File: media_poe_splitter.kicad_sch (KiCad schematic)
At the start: 81 parts, among them IC1 LAN7850-I_8JX, IC2 17791063215, IC3 93AA66C-I/SN, J1 Screw_Terminal_01x02, Q1 DMP3099L-7, X1 7499811120, X2 68710614522, Y1 830055299

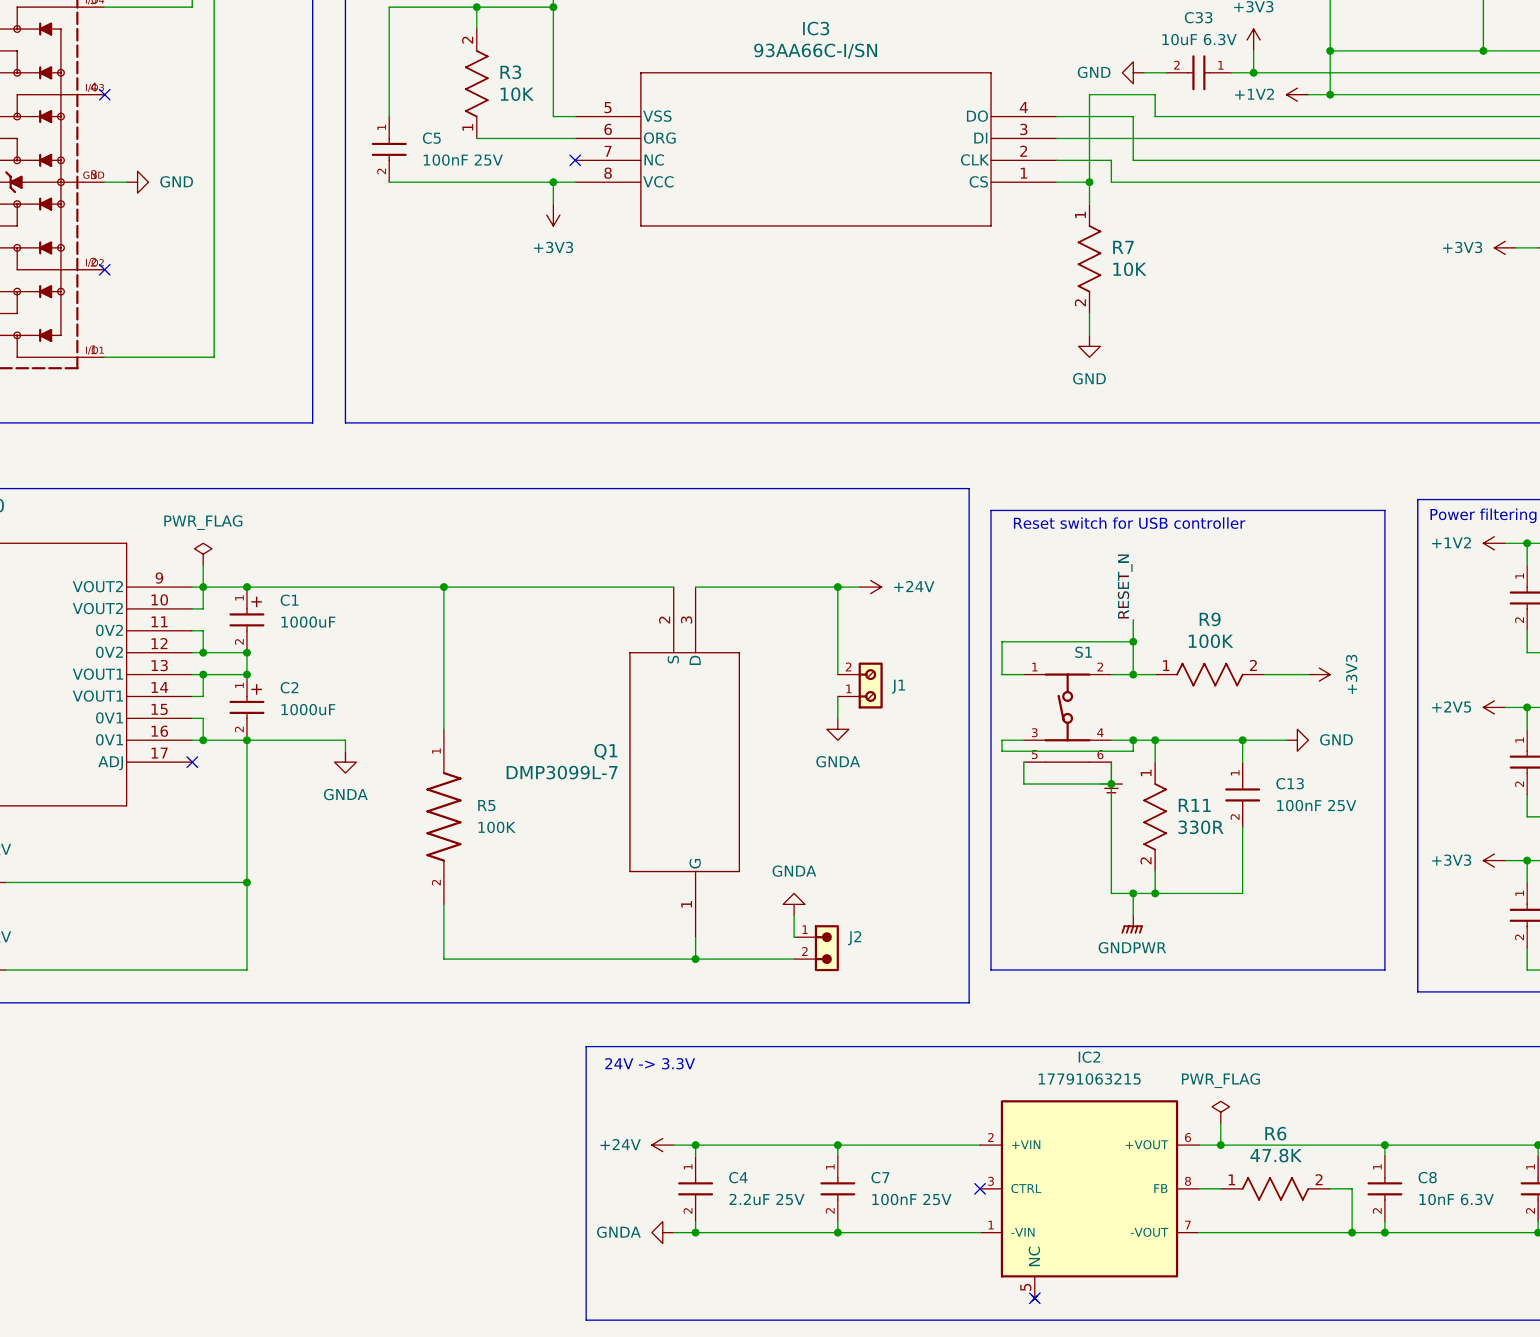
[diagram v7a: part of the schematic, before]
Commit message: board, schematic: try to comply with ERC and DRC
Signed-off-by: Marc 'risson' Schmitt <marc.schmitt@risson.space>
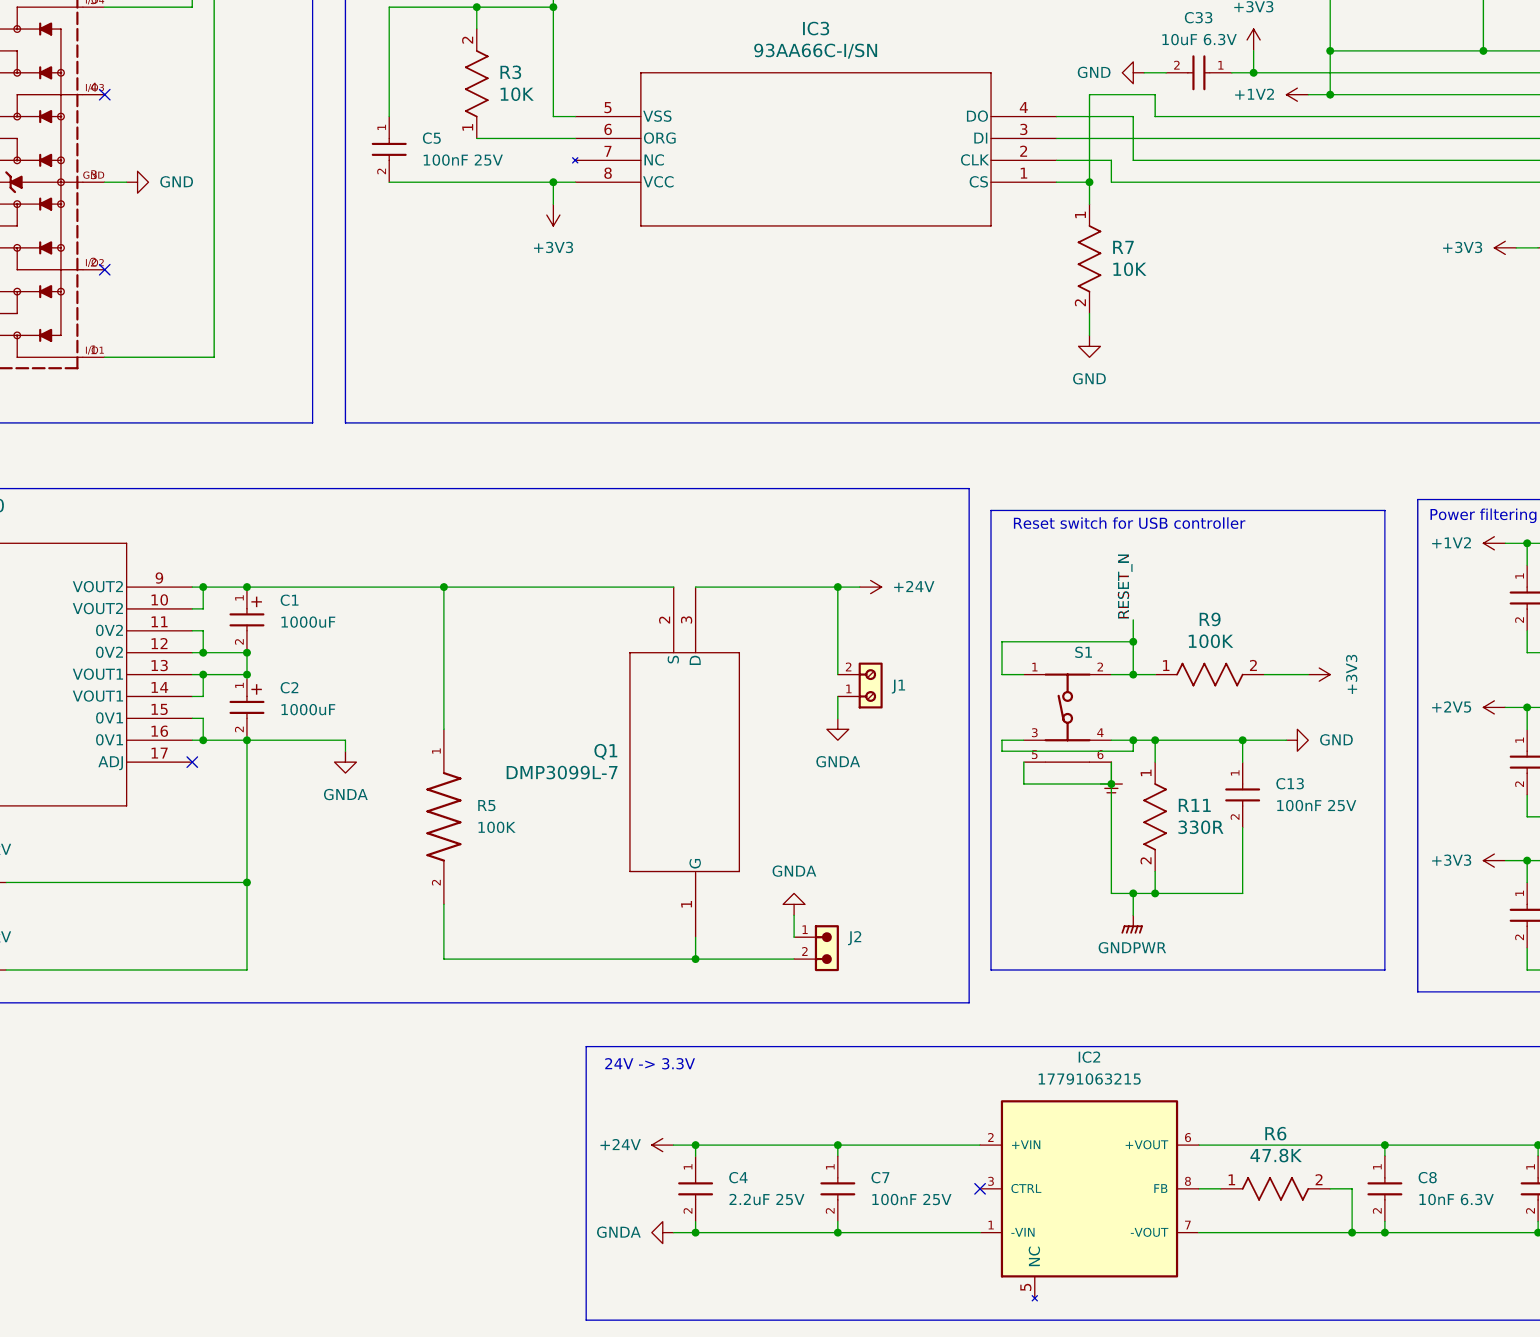
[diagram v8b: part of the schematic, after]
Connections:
- no-connect marks 35 -> 33
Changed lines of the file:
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@@
 	)
 	(junction
-		(at 311.15 276.86)
-		(diameter 0)
-		(color 0 0 0 0)
-	)
-	(junction
 		(at 100.33 116.84)
 		(diameter 0)
@@
 	)
 	(no_connect
-		(at 236.22 162.56)
-	)
-	(no_connect
 		(at 140.97 232.41)
 	)
@@
 	)
 	(no_connect
-		(at 289.56 294.64)
-	)
-	(no_connect
 		(at 457.2 201.93)
 	)
@@
 	(wire
 		(pts
-			(xy 311.15 276.86) (xy 330.2 276.86)
-		)
-		(stroke
-			(width 0)
-			(type default)
-		)
-	)
-	(wire
-		(pts
 			(xy 323.85 149.86) (xy 341.63 149.86)
 		)
@@
 	(wire
 		(pts
-			(xy 308.61 276.86) (xy 311.15 276.86)
+			(xy 308.61 276.86) (xy 330.2 276.86)
 		)
 		(stroke
@@
 	(wire
 		(pts
-			(xy 311.15 274.32) (xy 311.15 276.86)
-		)
-		(stroke
-			(width 0)
-			(type default)
-		)
-	)
-	(wire
-		(pts
 			(xy 359.41 256.54) (xy 372.11 256.54)
 		)
@@
 	(wire
 		(pts
-			(xy 193.04 209.55) (xy 193.04 212.09)
-		)
-		(stroke
-			(width 0)
-			(type default)
-		)
-	)
-	(wire
-		(pts
 			(xy 292.1 160.02) (xy 373.38 160.02)
 		)
@@
 	)
 	(symbol
-		(lib_id "power:PWR_FLAG")
-		(at 193.04 209.55 0)
-		(unit 1)
-		(exclude_from_sim no)
-		(in_bom yes)
-		(on_board yes)
-		(dnp no)
-		(fields_autoplaced yes)
-		(property "Reference" "#FLG01"
-			(at 193.04 207.645 0)
-			(effects
-				(font
-					(size 1.27 1.27)
-				)
-				(hide yes)
-			)
-		)
-		(property "Value" "PWR_FLAG"
-			(at 193.04 204.47 0)
-			(effects
-				(font
-					(size 1.27 1.27)
-				)
-			)
-		)
-		(property "Footprint" ""
-			(at 193.04 209.55 0)
-			(effects
-				(font
-					(size 1.27 1.27)
-				)
-				(hide yes)
-			)
-		)
-		(property "Datasheet" "~"
-			(at 193.04 209.55 0)
-			(effects
-				(font
-					(size 1.27 1.27)
-				)
-				(hide yes)
-			)
-		)
-		(property "Description" "Special symbol for telling ERC where power comes from"
-			(at 193.04 209.55 0)
-			(effects
-				(font
-					(size 1.27 1.27)
-				)
-				(hide yes)
-			)
-		)
-		(pin "1"
-		)
-		(instances
-			(project ""
-				(path "/6322d6ab-712b-4593-ad2b-135ce593cd38"
-					(reference "#FLG01")
-					(unit 1)
-				)
-			)
-		)
-	)
-	(symbol
 		(lib_id "885012206071:885012206071")
 		(at 214.63 160.02 270)
@@
 					(unit 1)
 				)
-			)
-		)
-	)
-	(symbol
-		(lib_id "power:PWR_FLAG")
-		(at 311.15 274.32 0)
-		(unit 1)
-		(exclude_from_sim no)
-		(in_bom yes)
-		(on_board yes)
-		(dnp no)
-		(fields_autoplaced yes)
-		(property "Reference" "#FLG02"
-			(at 311.15 272.415 0)
-			(effects
-				(font
-					(size 1.27 1.27)
-				)
-				(hide yes)
-			)
-		)
-		(property "Value" "PWR_FLAG"
-			(at 311.15 269.24 0)
-			(effects
-				(font
-					(size 1.27 1.27)
-				)
-			)
-		)
-		(property "Footprint" ""
-			(at 311.15 274.32 0)
-			(effects
-				(font
-					(size 1.27 1.27)
-				)
-				(hide yes)
-			)
-		)
-		(property "Datasheet" "~"
-			(at 311.15 274.32 0)
-			(effects
-				(font
-					(size 1.27 1.27)
-				)
-				(hide yes)
-			)
-		)
-		(property "Description" "Special symbol for telling ERC where power comes from"
-			(at 311.15 274.32 0)
-			(effects
-				(font
-					(size 1.27 1.27)
-				)
-				(hide yes)
-			)
-		)
-		(pin "1"
-		)
-		(instances
-			(project ""
-				(path "/6322d6ab-712b-4593-ad2b-135ce593cd38"
-					(reference "#FLG02")
-					(unit 1)
-				)
